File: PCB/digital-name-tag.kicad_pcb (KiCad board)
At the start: 2 copper layers, 99 x 99 mm, 18 parts, among them J1 Conn_01x04, SW1 SW_Push, SW2 SW_Push, SW3 SW_Push, SW4 SW_Push

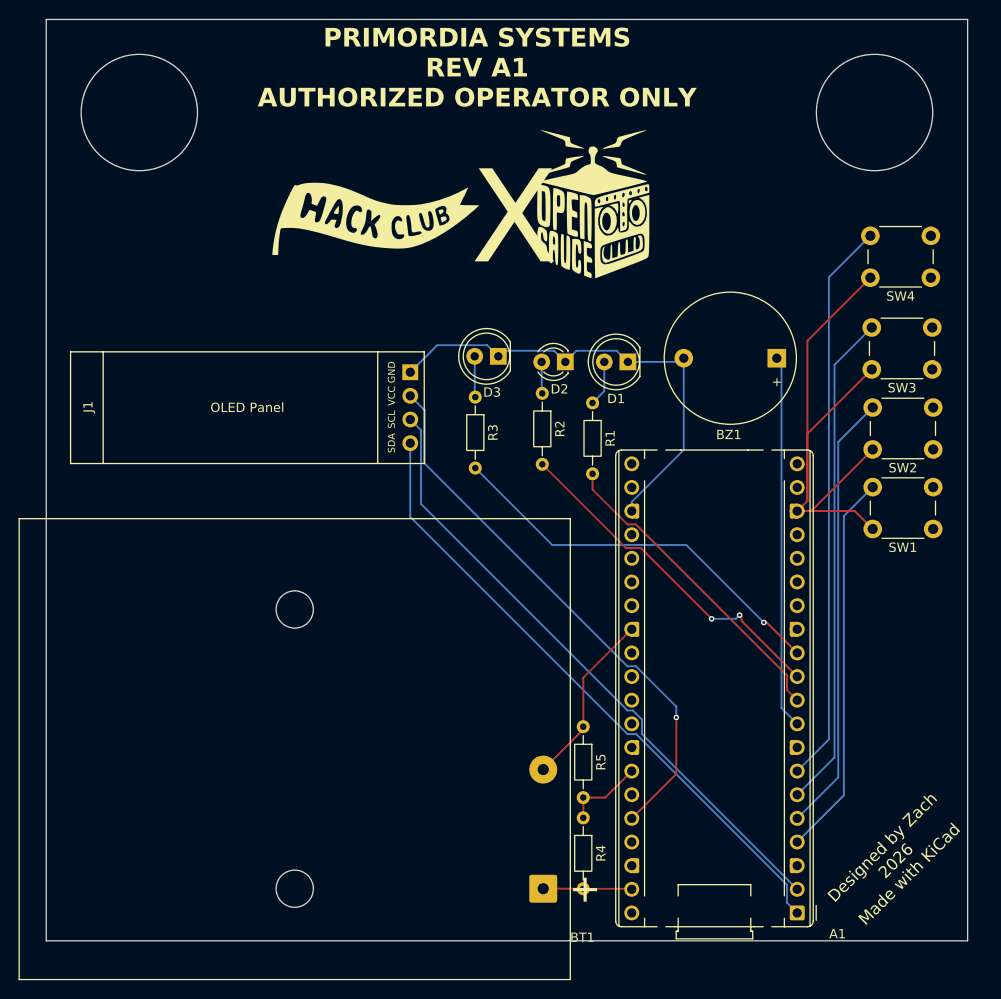
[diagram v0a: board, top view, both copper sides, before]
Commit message: added a image of the 3d model and updated battery holder footprint to be a 3xAAA holder
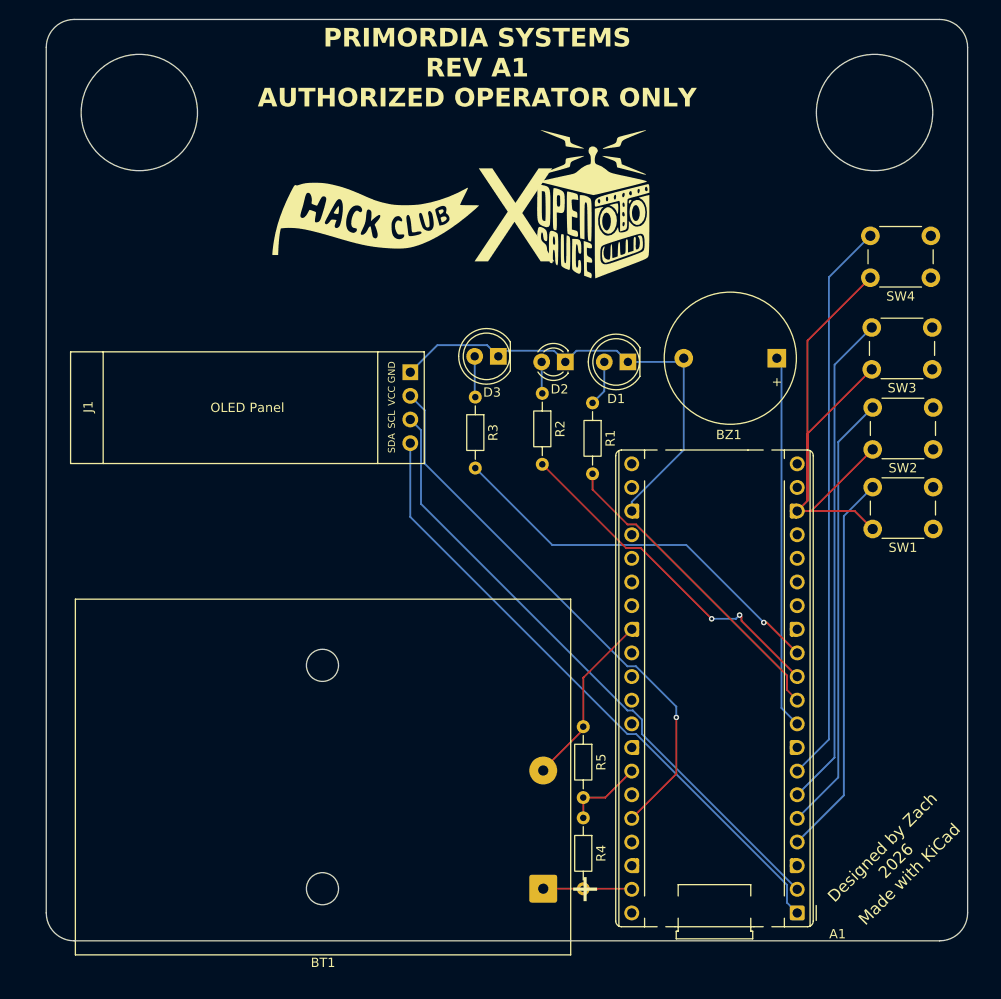
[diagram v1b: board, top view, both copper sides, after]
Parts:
- BT1: footprint Battery:BatteryHolder_TruPower_BH-331P_3xAA -> Battery:BatteryHolder_Keystone_2479_3xAAA
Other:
- outline, holes or cut-outs redrawn
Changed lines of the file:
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@@
 		)
 	)
-	(footprint "Battery:BatteryHolder_TruPower_BH-331P_3xAA"
+	(footprint "Battery:BatteryHolder_Keystone_2479_3xAAA"
 		(layer "F.Cu")
 		(at 152.3 119.2 180)
-		(descr "Battery holder, TruPower BH-331P, battery type 3xAA, https://static.rapidonline.com/pdf/18-2967_v1.pdf, generated with kicad-footprint-generator StandardBox_generator.py")
+		(descr "Battery holder, Keystone 2479, battery type 3xAAA, http://www.keyelco.com/product-pdf.cfm?p=1041, generated with kicad-footprint-generator StandardBox_generator.py")
 		(tags "horizontal triple")
 		(property "Reference" "BT1"
-			(at -4.21 -5.25 0)
+			(at 23.66 -7.95 180)
 			(layer "F.SilkS")
 			(effects
 				(font
 					(size 1 1)
-					(thickness 2)
+					(thickness 0.15)
 				)
 			)
 		)
 		(property "Value" "Battery"
-			(at 26.7 40.6 0)
+			(at 23.66 31.95 180)
 			(layer "F.Fab")
 			(effects
@@
 			)
 		)
-		(property "Datasheet" "~"
-			(at 0 0 0)
+		(property "Datasheet" ""
+			(at 0 0 180)
 			(layer "F.Fab")
 			(hide yes)
@@
 			)
 		)
-		(property "Description" "Multiple-cell battery"
-			(at 0 0 0)
+		(property "Description" ""
+			(at 0 0 180)
 			(layer "F.Fab")
 			(hide yes)
@@
 		(attr through_hole)
 		(fp_line
-			(start 56.31 39.76)
-			(end -2.91 39.76)
+			(start 50.27 31.11)
+			(end -2.95 31.11)
 			(stroke
 				(width 0.12)
@@
 		)
 		(fp_line
-			(start 56.31 -9.76)
-			(end 56.31 39.76)
+			(start 50.27 -7.11)
+			(end 50.27 31.11)
 			(stroke
 				(width 0.12)
@@
 		)
 		(fp_line
-			(start -2.91 39.76)
-			(end -2.91 -9.76)
+			(start -2.95 31.11)
+			(end -2.95 -7.11)
 			(stroke
 				(width 0.12)
@@
 		)
 		(fp_line
-			(start -2.91 -9.76)
-			(end 56.31 -9.76)
+			(start -2.95 -7.11)
+			(end 50.27 -7.11)
 			(stroke
 				(width 0.12)
@@
 		)
 		(fp_rect
-			(start -3.05 -9.9)
-			(end 56.45 39.9)
+			(start -3.09 -7.25)
+			(end 50.41 31.25)
 			(stroke
 				(width 0.05)
@@
 		)
 		(fp_rect
-			(start -2.3 -9.15)
-			(end 55.7 39.15)
+			(start -2.59 -6.75)
+			(end 49.91 30.75)
 			(stroke
 				(width 0.1)
@@
 		)
 		(fp_text user "+"
-			(at -4.5 0 0)
+			(at -4.5 0.05 180)
 			(layer "F.SilkS")
 			(effects
 				(font
 					(size 3 3)
-					(thickness 2)
+					(thickness 0.15)
 				)
 			)
 		)
 		(fp_text user "${REFERENCE}"
-			(at 26.7 15 0)
+			(at 23.66 12 180)
 			(layer "F.Fab")
 			(effects
@@
 		)
 		(pad "" np_thru_hole circle
-			(at 26.7 0 180)
-			(size 4 4)
-			(drill 4)
+			(at 23.72 0 180)
+			(size 3.45 3.45)
+			(drill 3.45)
 			(layers "*.Cu" "*.Mask")
 		)
 		(pad "" np_thru_hole circle
-			(at 26.7 30 180)
-			(size 4 4)
-			(drill 4)
+			(at 23.72 24 180)
+			(size 3.45 3.45)
+			(drill 3.45)
 			(layers "*.Cu" "*.Mask")
 		)
@@
 			(at 0 0 180)
 			(size 3 3)
-			(drill 1.2)
+			(drill 1.1)
 			(layers "*.Cu" "*.Mask")
 			(remove_unused_layers no)
@@
 		)
 		(pad "2" thru_hole circle
-			(at 0 12.8 180)
+			(at 0 12.7 180)
 			(size 3 3)
-			(drill 1.2)
+			(drill 1.1)
 			(layers "*.Cu" "*.Mask")
 			(remove_unused_layers no)
@@
 		)
 		(embedded_fonts no)
-		(model "${KICAD9_3DMODEL_DIR}/Battery.3dshapes/BatteryHolder_TruPower_BH-331P_3xAA.step"
+		(model "${KICAD9_3DMODEL_DIR}/Battery.3dshapes/BatteryHolder_Keystone_2479_3xAAA.step"
 			(offset
 				(xyz 0 0 0)
@@
 		(layer "Edge.Cuts")
 	)
-	(gr_rect
-		(start 98.9 25.8)
-		(end 197.9 124.8)
+	(gr_line
+		(start 101.9 25.8)
+		(end 194.9 25.8)
+		(stroke
+			(width 0.05)
+			(type default)
+		)
+		(layer "Edge.Cuts")
+	)
+	(gr_arc
+		(start 194.9 25.8)
+		(mid 197.02132 26.67868)
+		(end 197.9 28.8)
+		(stroke
+			(width 0.05)
+			(type default)
+		)
+		(layer "Edge.Cuts")
+	)
+	(gr_arc
+		(start 197.9 121.8)
+		(mid 197.02132 123.92132)
+		(end 194.9 124.8)
+		(stroke
+			(width 0.05)
+			(type default)
+		)
+		(layer "Edge.Cuts")
+	)
+	(gr_line
+		(start 194.9 124.8)
+		(end 101.9 124.8)
+		(stroke
+			(width 0.05)
+			(type default)
+		)
+		(layer "Edge.Cuts")
+	)
+	(gr_arc
+		(start 101.9 124.8)
+		(mid 99.77868 123.92132)
+		(end 98.9 121.8)
+		(stroke
+			(width 0.05)
+			(type default)
+		)
+		(layer "Edge.Cuts")
+	)
+	(gr_line
+		(start 197.9 28.8)
+		(end 197.9 121.8)
+		(stroke
+			(width 0.05)
+			(type default)
+		)
+		(layer "Edge.Cuts")
+	)
+	(gr_arc
+		(start 98.9 28.8)
+		(mid 99.77868 26.67868)
+		(end 101.9 25.8)
+		(stroke
+			(width 0.05)
+			(type default)
+		)
+		(layer "Edge.Cuts")
+	)
+	(gr_line
+		(start 98.9 121.8)
+		(end 98.9 28.8)
 		(stroke
 			(width 0.05)
 			(type default)
 		)
-		(fill no)
 		(layer "Edge.Cuts")
 	)

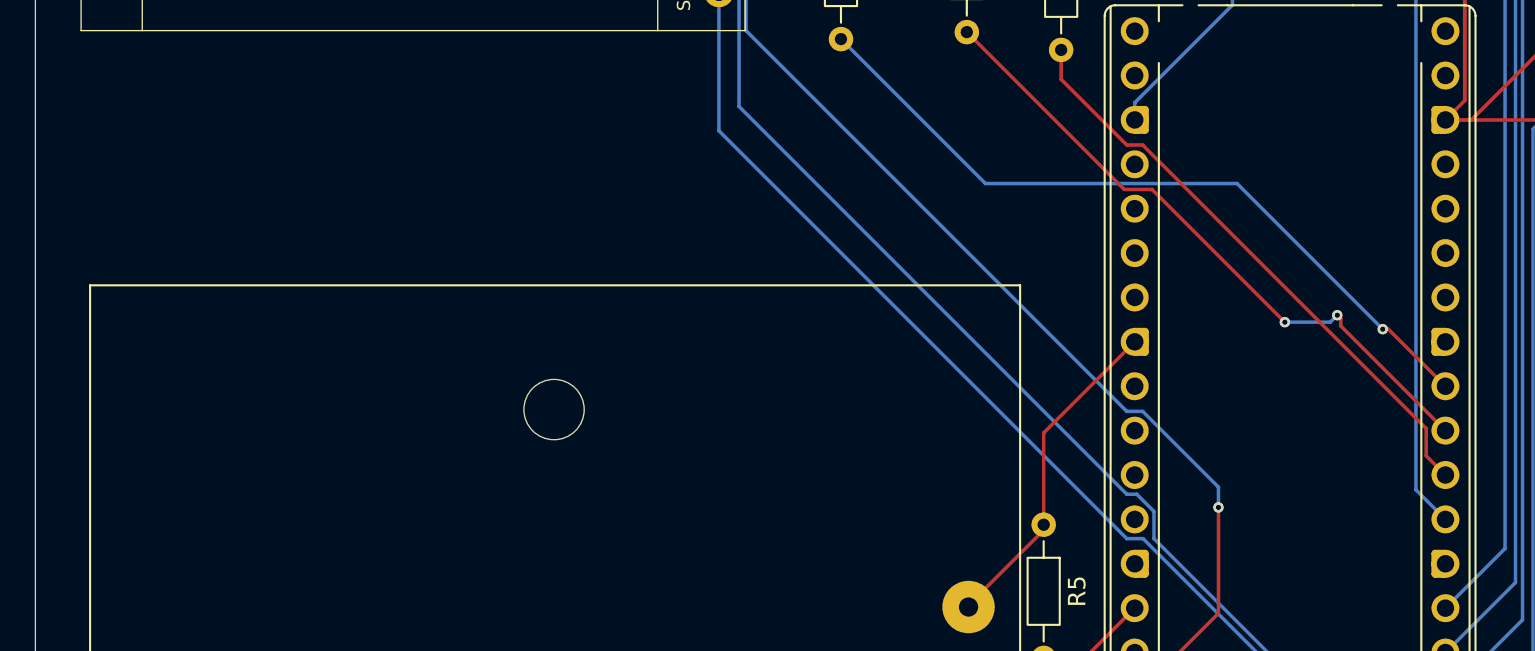
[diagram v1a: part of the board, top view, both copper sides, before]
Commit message: added more silkscreen art
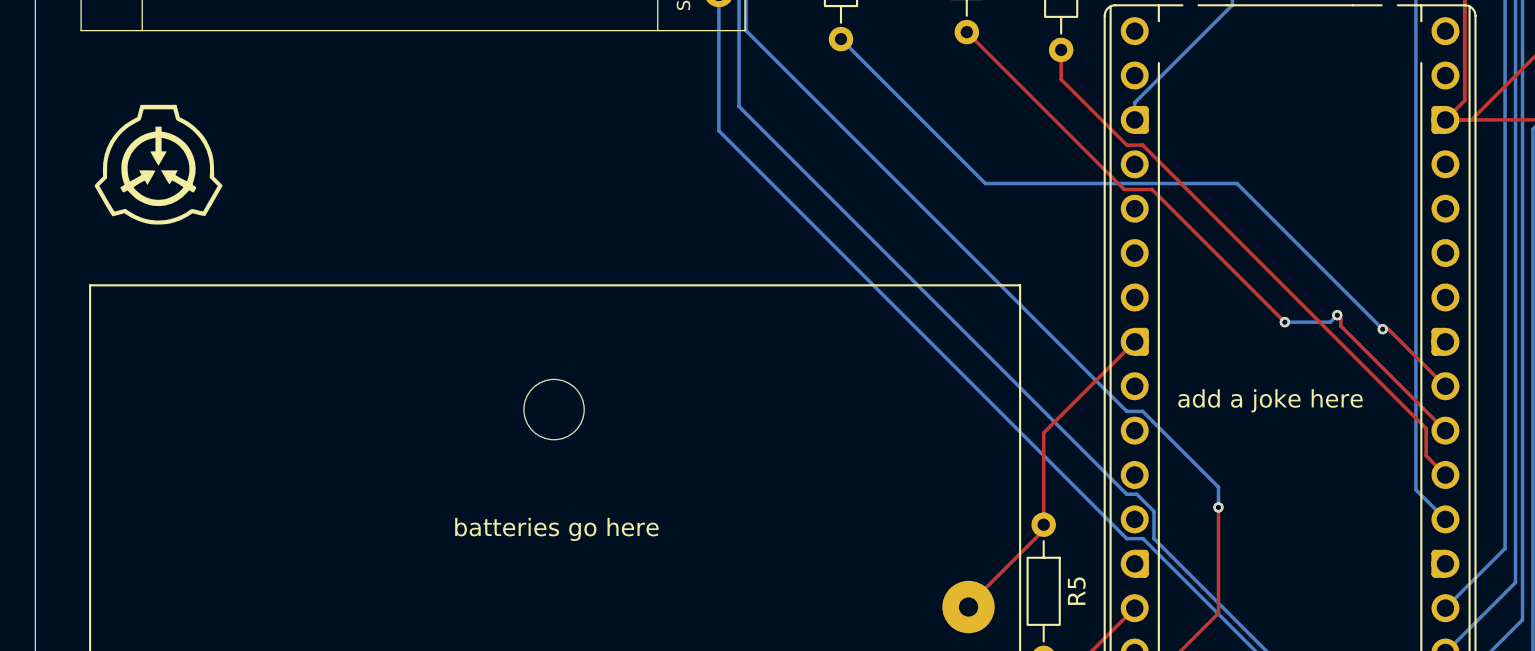
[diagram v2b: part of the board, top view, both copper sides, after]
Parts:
- added G***: LOGO, LOGO, F.Cu at (105.9, 81.2)
- added G***: LOGO, LOGO, B.Cu at (144.2, 107.2)
- added G***: LOGO, LOGO, B.Cu at (116.7, 68.4)
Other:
- board text added: "add a joke here"
- board text added: "batteries go here"
- board text added: "parts go on the other side"
